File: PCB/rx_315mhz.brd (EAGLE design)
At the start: 80 x 35 mm, 5 parts

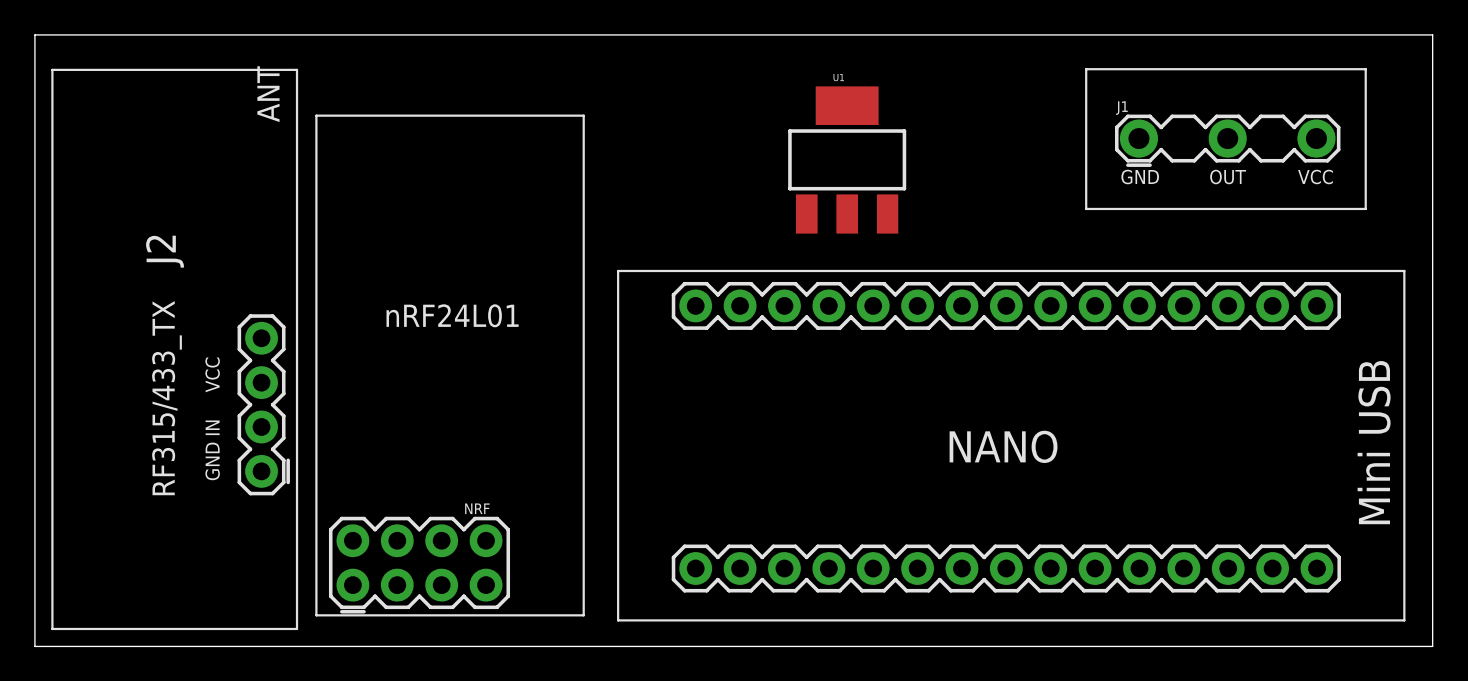
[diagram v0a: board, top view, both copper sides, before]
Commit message: pcb_out,arduino struct
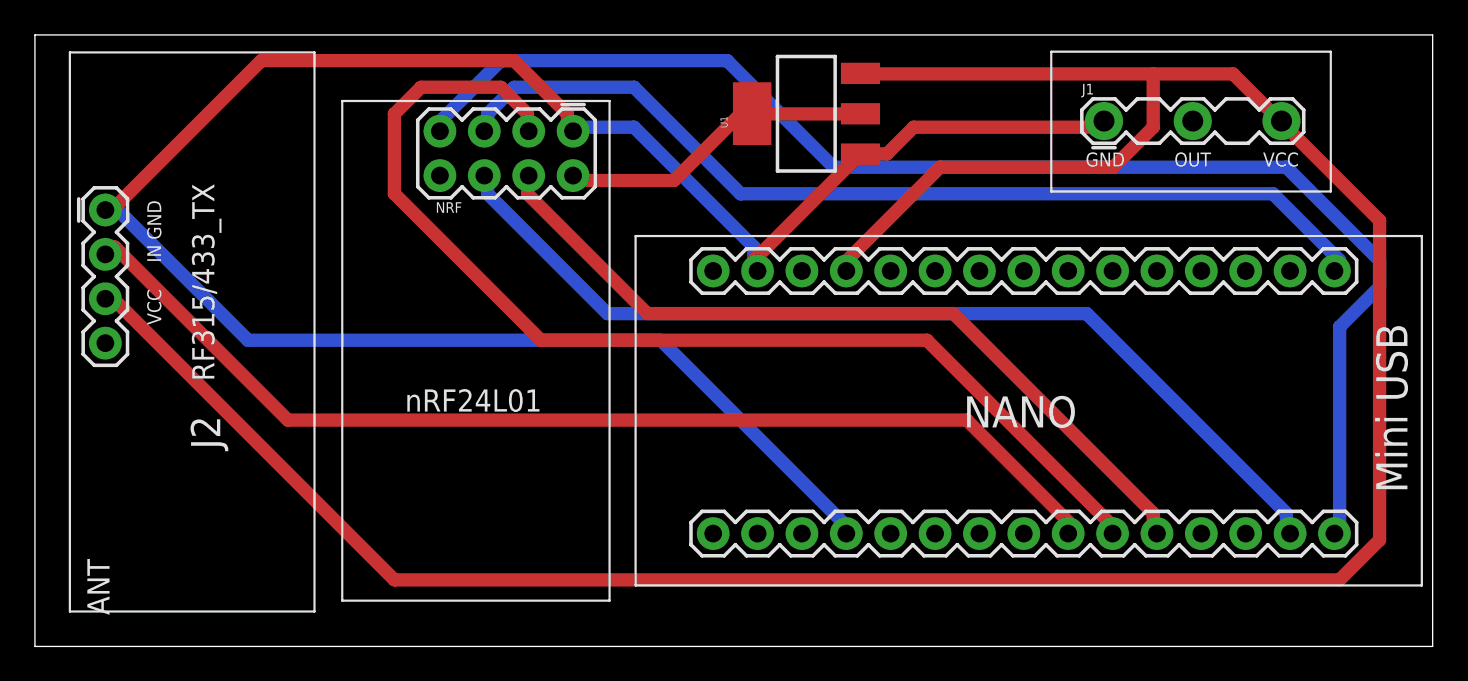
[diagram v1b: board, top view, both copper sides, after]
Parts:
- moved J2 35.5 mm to (2.00, 34.0), turned to 270 degrees
- moved NRF 32.5 mm to (17.6, 31.2), turned to 180 degrees
- moved U1 3.53 mm to (44.1, 30.5), turned to 90 degrees
- moved NANO 2.24 mm to (64.2, 13.4)
- moved J1 2.24 mm to (58.2, 26.0)
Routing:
- net +5V: track 0.00 -> 156.3 mm
- net GND: track 0.00 -> 121.5 mm
- net D12: track 0.00 -> 77.5 mm
- net D7: track 0.00 -> 63.9 mm
- net D6: track 0.00 -> 62.7 mm
- net D11: track 0.00 -> 55.6 mm
- net D13: track 0.00 -> 55.2 mm
- net D8: track 0.00 -> 45.7 mm
- net +3.3V: track 0.00 -> 18.1 mm
